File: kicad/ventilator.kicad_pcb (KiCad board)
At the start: 2 copper layers, 44 parts, among them J1 Conn_01x02, J2 Conn_01x02, J3 Conn_01x02, J4 Conn_01x02, J5 Conn_01x02, J6 Conn_01x02, Q1 IRLIZ44NPBF, Q2 IRLIZ44NPBF, Q3 IRLIZ44NPBF, Q4 IRLIZ44NPBF, Q5 IRLIZ44NPBF, Q6 IRLIZ44NPBF

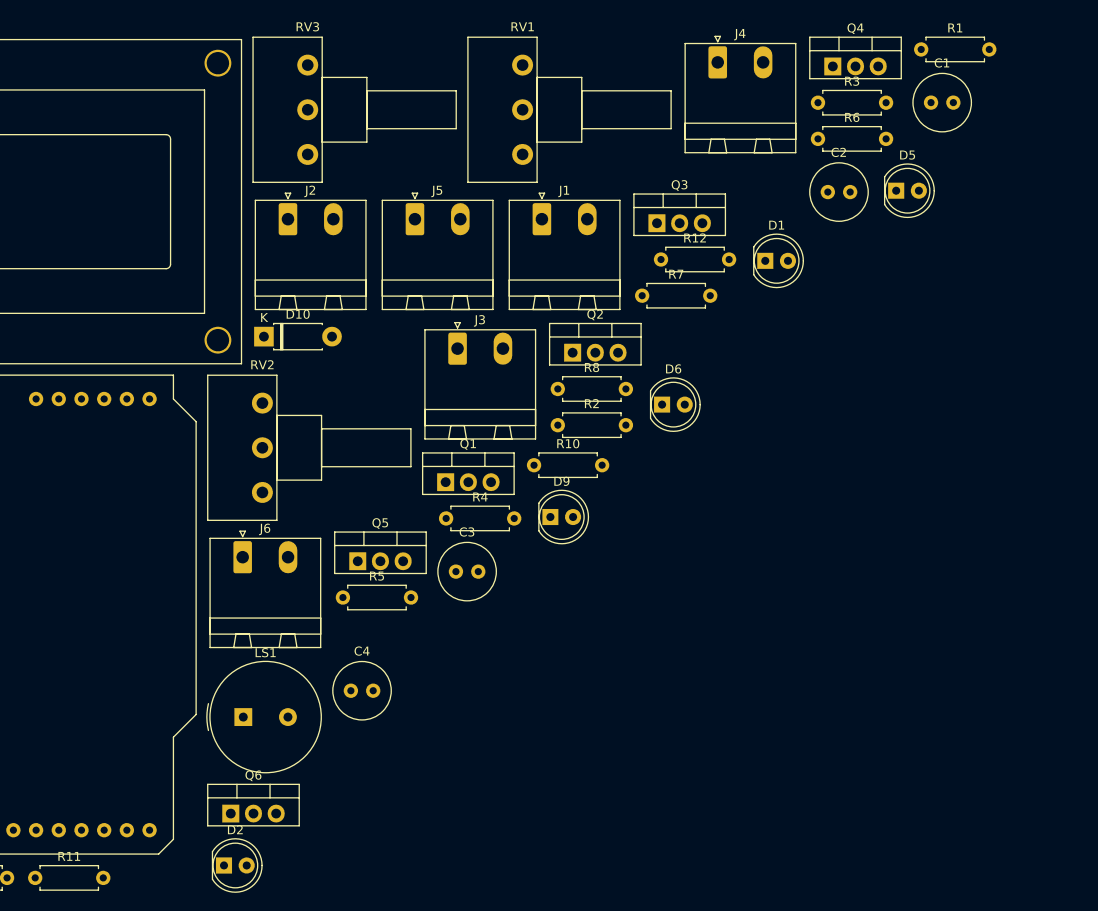
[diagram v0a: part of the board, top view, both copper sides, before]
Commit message: modifies schematic with new pin mapping
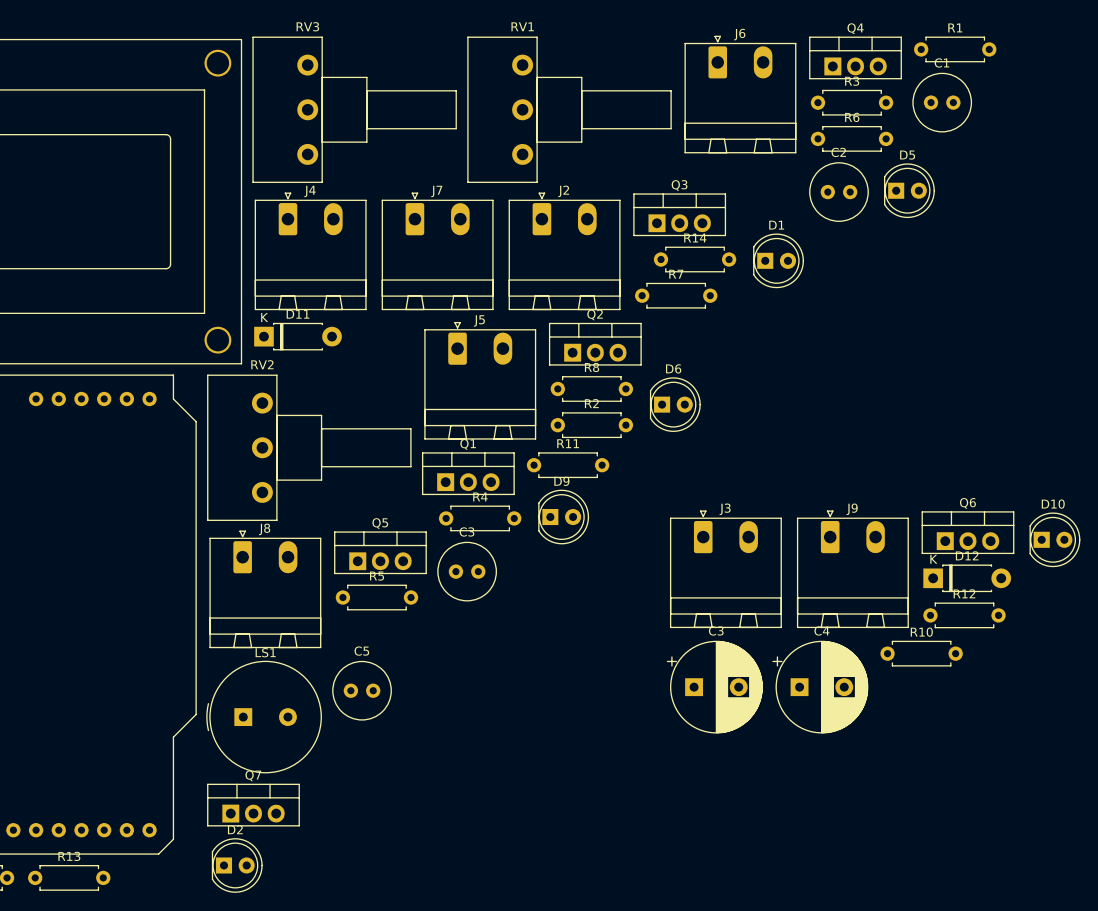
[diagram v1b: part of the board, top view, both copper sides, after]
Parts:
- added C3: 680uF 25V, Capacitor_THT:CP_Radial_D10.0mm_P5.00mm, F.Cu at (203.8, 128.2)
- added C4: 680uF 25V, Capacitor_THT:CP_Radial_D10.0mm_P5.00mm, F.Cu at (215.6, 128.2)
- added D10: LED, LED_THT:LED_D5.0mm, F.Cu at (242.7, 111.8)
- added D12: 1N4004, Diode_THT:D_DO-41_SOD81_P7.62mm_Horizontal, F.Cu at (230.5, 116.1)
- added J3: Conn_01x02, Connector_Phoenix_MSTB:PhoenixContact_MSTBA_2,5_2-G-5,08_1x02_P5.08mm_Horizontal, F.Cu at (204.8, 111.5)
- added J9: Conn_01x02, Connector_Phoenix_MSTB:PhoenixContact_MSTBA_2,5_2-G-5,08_1x02_P5.08mm_Horizontal, F.Cu at (219.0, 111.5)
- added Q6: IRLIZ44NPBF, Package_TO_SOT_THT:TO-220-3_Vertical, F.Cu at (231.9, 111.9)
- added R10: 1K, Resistor_THT:R_Axial_DIN0207_L6.3mm_D2.5mm_P7.62mm_Horizontal, F.Cu at (225.4, 124.5)
- added R12: 10K, Resistor_THT:R_Axial_DIN0207_L6.3mm_D2.5mm_P7.62mm_Horizontal, F.Cu at (230.2, 120.2)
- renumbered C4 to C5, D10 to D11, J1 to J2, J2 to J4, J3 to J5, J4 to J6, J5 to J7, J6 to J8, Q6 to Q7, R10 to R11, R11 to R13, R12 to R14
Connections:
- net /LCD_D4 renamed /LCD_DIO4
- A1 pad 12: Net-(A1-Pad12) -> /BUZZER
- A1 pad 18: /LCD_D5 -> /FILL_CLOSE
- A1 pad 19: /LCD_D6 -> /LCD_DIO5
- A1 pad 20: /LCD_D7 -> /INS_CLOSE
- A1 pad 21: /EXP_OPEN -> /EXP_CLOSE
- A1 pad 22: /BUZZER -> /LCD_DIO6
- A1 pad 23: /EXP_CLOSE -> /LCD_DIO7
- A1 pad 24: /INS_OPEN -> /EXP_OPEN
- A1 pad 26: /LCD_E -> /FILL_OPEN
- A1 pad 28: /INS_CLOSE -> /LCD_EN
- DS1 pad 12: /LCD_D5 -> /LCD_DIO5
- DS1 pad 13: /LCD_D6 -> /LCD_DIO6
- DS1 pad 14: /LCD_D7 -> /LCD_DIO7
- DS1 pad 6: /LCD_E -> /LCD_EN
- Q5 pad 1: /FILL -> /FILL_CLOSE
- R11 pad 1: /FILL -> /FILL_CLOSE
- R9 pad 2: /FILL -> /FILL_CLOSE

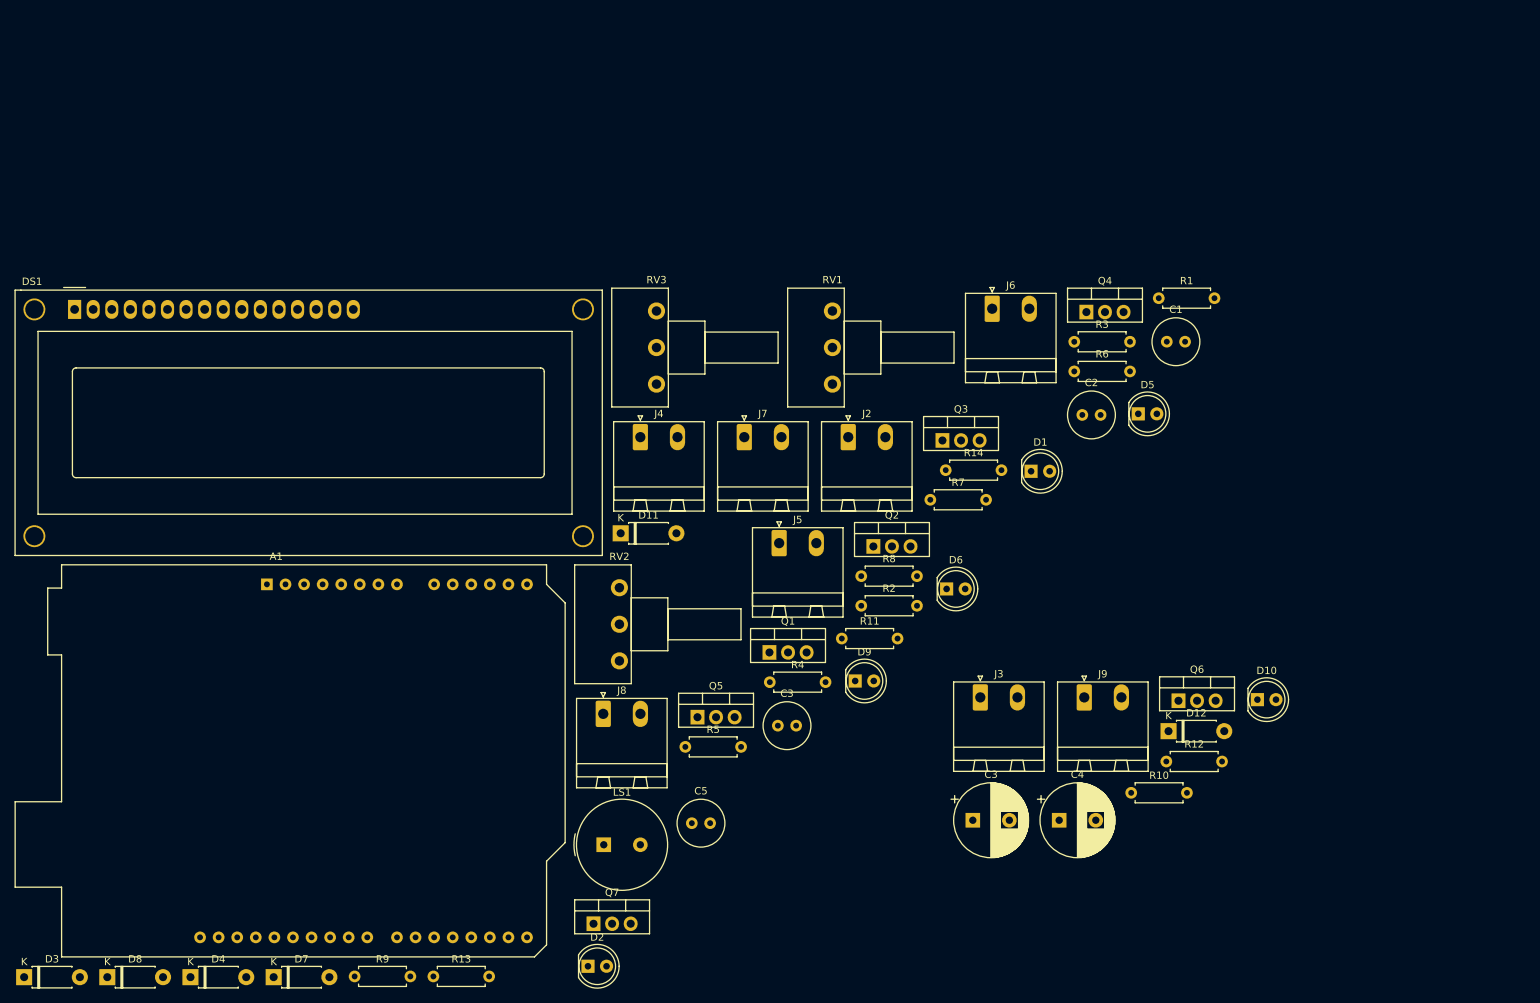
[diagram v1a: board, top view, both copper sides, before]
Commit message: finishes basic kicad board layout
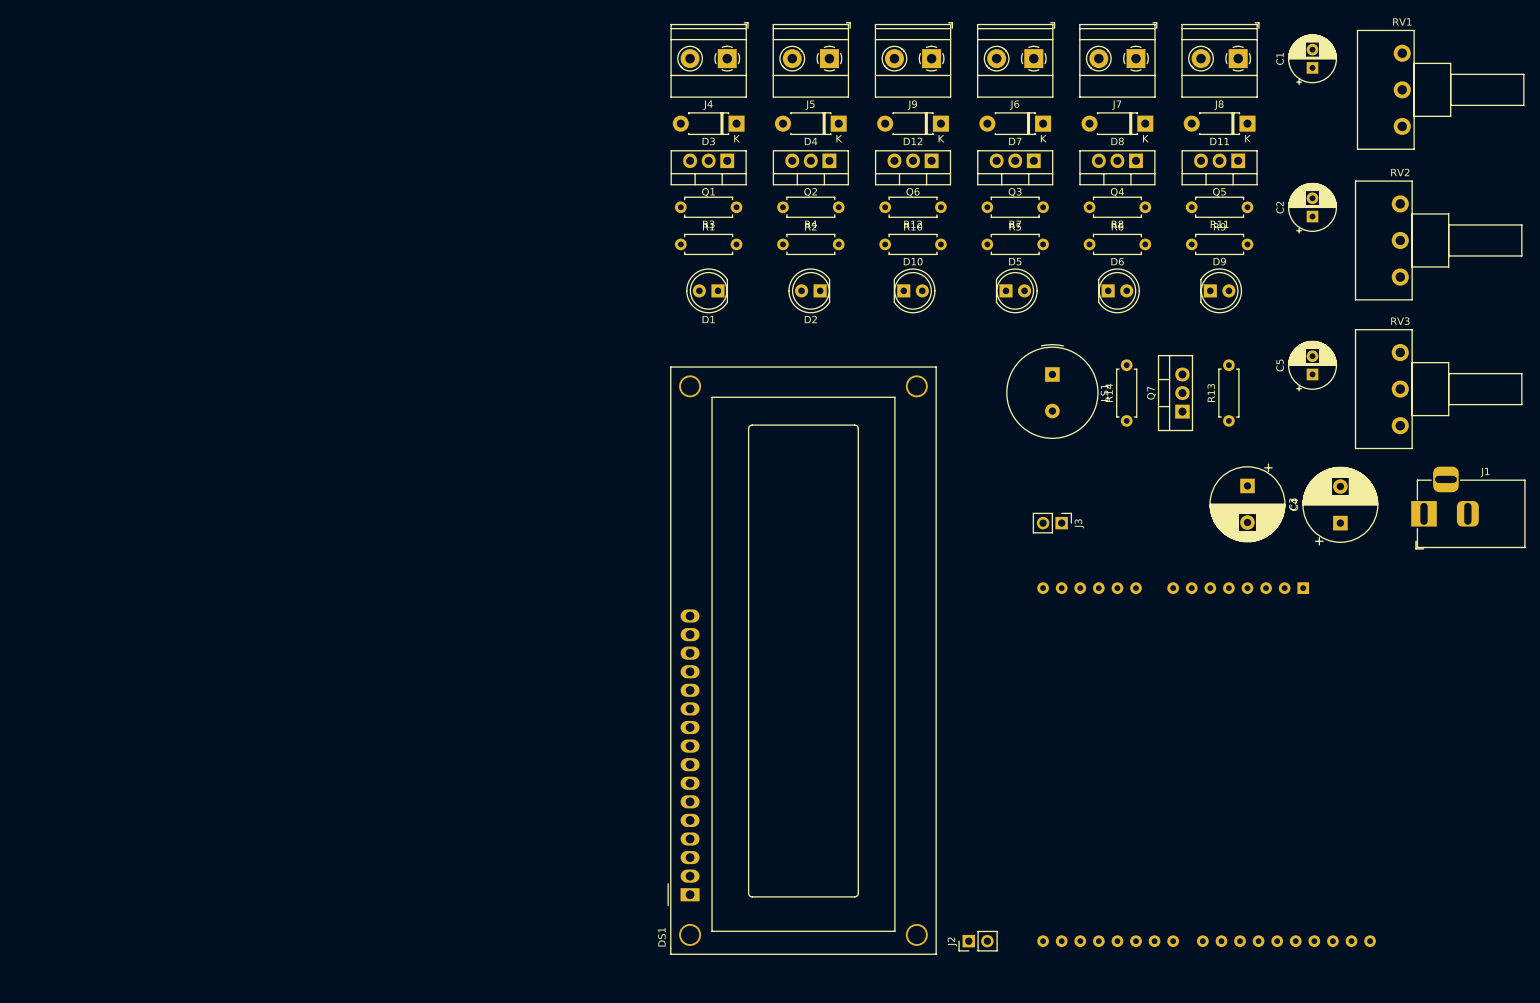
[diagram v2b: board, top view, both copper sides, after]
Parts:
- removed the C3 at (177.1, 115.3)
- added J1: PJ-202A, Connector_BarrelJack:BarrelJack_Horizontal, F.Cu at (265.4, 86.4)
- A1: moved to B.Cu
- C1, C2, C5: footprint Capacitor_THT:C_Radial_D6.3mm_H5.0mm_P2.50mm -> Capacitor_THT:CP_Radial_D6.3mm_P2.50mm
- J2, J3: footprint Connector_Phoenix_MSTB:PhoenixContact_MSTBA_2,5_2-G-5,08_1x02_P5.08mm_Horizontal -> Connector_PinHeader_2.54mm:PinHeader_1x02_P2.54mm_Vertical
- J4, J5, J6, J7, J8, J9: footprint Connector_Phoenix_MSTB:PhoenixContact_MSTBA_2,5_2-G-5,08_1x02_P5.08mm_Horizontal -> TerminalBlock_Phoenix:TerminalBlock_Phoenix_MKDS-1,5-2-5.08_1x02_P5.08mm_Horizontal
- moved D8 183.7 mm to (227.3, 33.0), turned to 180 degrees
- moved D7 157.1 mm to (213.4, 33.0), turned to 180 degrees
- moved R9 152.0 mm to (233.7, 49.5)
- moved D3 152.0 mm to (171.4, 33.0), turned to 180 degrees
- moved D4 146.5 mm to (185.4, 33.0), turned to 180 degrees
- moved A1 141.7 mm to (248.9, 96.5), turned to 180 degrees
- moved R13 132.6 mm to (238.8, 73.7), turned to 90 degrees
- moved J8 124.7 mm to (240.0, 24.1), turned to 180 degrees
- moved RV2 118.9 mm to (262.2, 54.0)
- moved DS1 116.1 mm to (165.1, 138.4), turned to 90 degrees
- moved Q7 106.7 mm to (232.4, 72.4), turned to 90 degrees
- moved Q5 106.1 mm to (240.0, 38.1), turned to 180 degrees
- moved C5 104.7 mm to (250.2, 67.3), turned to 90 degrees
- moved D11 102.4 mm to (241.3, 33.0), turned to 180 degrees
- moved RV3 101.8 mm to (262.2, 74.3)
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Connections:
- C1 pad 1: GND -> /POT_0
- C1 pad 2: /POT_0 -> GND
- C2 pad 1: GND -> /POT_1
- C2 pad 2: /POT_1 -> GND
- C5 pad 1: GND -> /POT_2
- C5 pad 2: /POT_2 -> GND
